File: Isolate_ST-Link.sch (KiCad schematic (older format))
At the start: 54 parts, among them J1 USB_OTG, J2 CONN_01X06, J3 CONN_01X04, J4 CONN_01X02, J5 CONN_01X02, Q1 BSS138, U1 MAU10x, U2 ADuM4160, U3 APE8865NR-33-HF-3

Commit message: 10pin版つくった
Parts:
- removed J2: CONN_01X06, Connector_JST:JST_EH_S06B-EH_1x06_P2.50mm_Horizontal, symbol Isolate_ST-Link-rescue:CONN_01X06
- added J2: Conn_02x05_Odd_Even, Connector_PinHeader_1.27mm:PinHeader_2x05_P1.27mm_Vertical_SMD, symbol Connector_Generic:Conn_02x05_Odd_Even
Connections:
- wire segments 165 -> 177
- no-connect marks 1 -> 3
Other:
- moved on the sheet: R28
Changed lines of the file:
@@
 	1    0    0    -1
-$EndComp
-$Comp
-L Isolate_ST-Link-rescue:CONN_01X06 J2
-U 1 1 5948A2BD
-P 9500 2950
-F 0 "J2" H 9500 3300 50  0000 C CNN
-F 1 "CONN_01X06" V 9600 2950 50  0000 C CNN
-F 2 "Connector_JST:JST_EH_S06B-EH_1x06_P2.50mm_Horizontal" H 9500 2950 50  0001 C CNN
-F 3 "" H 9500 2950 50  0001 C CNN
-	1    9500 2950
-	1    0    0    1
 $EndComp
 Text GLabel 8000 2700 0    60   Input ~ 0
@@
 Text GLabel 8000 2900 0    60   Input ~ 0
 T_JTMS
-$Comp
-L power1:GND #PWR08
-U 1 1 5948BBA0
-P 8800 3250
-F 0 "#PWR08" H 8800 3000 50  0001 C CNN
-F 1 "GND" H 8800 3100 50  0000 C CNN
-F 2 "" H 8800 3250 50  0001 C CNN
-F 3 "" H 8800 3250 50  0001 C CNN
-	1    8800 3250
-	-1   0    0    -1
-$EndComp
-Text GLabel 8000 3100 0    60   Input ~ 0
+Text GLabel 8000 3000 0    60   Input ~ 0
 T_JTCK
 $Comp
@@
 L device:R R28
 U 1 1 59CA9CFA
-P 8550 3100
-F 0 "R28" V 8630 3100 50  0000 C CNN
-F 1 "22" V 8550 3100 50  0000 C CNN
-F 2 "Resistor_SMD:R_0603_1608Metric" V 8480 3100 50  0001 C CNN
-F 3 "" H 8550 3100 50  0001 C CNN
-	1    8550 3100
+P 8550 3000
+F 0 "R28" V 8630 3000 50  0000 C CNN
+F 1 "22" V 8550 3000 50  0000 C CNN
+F 2 "Resistor_SMD:R_0603_1608Metric" V 8480 3000 50  0001 C CNN
+F 3 "" H 8550 3000 50  0001 C CNN
+	1    8550 3000
 	0    -1   1    0
 $EndComp
@@
 Connection ~ 1250 4700
 Wire Wire Line
-	8800 3000 9300 3000
-Wire Wire Line
 	6150 4800 6200 4800
 Wire Wire Line
 	6200 5100 6150 5100
 Wire Wire Line
-	7450 3200 8900 3200
+	7450 3200 9700 3200
 Wire Wire Line
 	8000 2900 8100 2900
@@
 Connection ~ 1600 4050
 Wire Wire Line
-	8700 3100 9000 3100
+	8700 3000 9000 3000
 Wire Wire Line
 	8400 2900 9100 2900
@@
 	8800 2000 9200 2000
 Wire Wire Line
-	8900 2450 8900 3200
-Connection ~ 8900 3200
-Wire Wire Line
-	8400 2700 9300 2700
+	9700 2450 9700 3200
 Wire Wire Line
 	9200 2000 9200 2800
-Connection ~ 9200 2800
 Wire Wire Line
 	9100 2150 9100 2900
-Connection ~ 9100 2900
-Wire Wire Line
-	9000 2300 9000 3100
-Connection ~ 9000 3100
+Wire Wire Line
+	9000 2300 9000 3000
 Wire Notes Line
 	3800 2400 3800 5050
@@
 Connection ~ 6200 4800
 Wire Wire Line
-	8000 3100 8400 3100
-Wire Wire Line
-	8900 2450 8800 2450
+	8000 3000 8400 3000
+Wire Wire Line
+	9700 2450 8800 2450
 Wire Wire Line
 	8500 2450 7700 2450
@@
 	7700 2450 7700 1800
 Wire Wire Line
-	8800 3250 8800 3000
-Wire Wire Line
 	8150 4450 8750 4450
 Wire Wire Line
@@
 	1600 4050 1650 4050
 Wire Wire Line
-	8900 3200 9300 3200
-Wire Wire Line
-	9200 2800 9300 2800
-Wire Wire Line
-	9100 2900 9300 2900
-Wire Wire Line
-	9000 3100 9300 3100
-Wire Wire Line
 	9000 3700 9000 4350
 Wire Wire Line
@@
 Wire Wire Line
 	6200 4800 6200 5100
+$Comp
+L Connector_Generic:Conn_02x05_Odd_Even J2
+U 1 1 5C6B4233
+P 10100 3400
+F 0 "J2" H 10150 3817 50  0000 C CNN
+F 1 "Conn_02x05_Odd_Even" H 10150 3726 50  0000 C CNN
+F 2 "Connector_PinHeader_1.27mm:PinHeader_2x05_P1.27mm_Vertical_SMD" H 10100 3400 50  0001 C CNN
+F 3 "~" H 10100 3400 50  0001 C CNN
+	1    10100 3400
+	1    0    0    -1
+$EndComp
+$Comp
+L power1:GND #PWR0101
+U 1 1 5C6B457F
+P 9800 3650
+F 0 "#PWR0101" H 9800 3400 50  0001 C CNN
+F 1 "GND" H 9800 3500 50  0000 C CNN
+F 2 "" H 9800 3650 50  0001 C CNN
+F 3 "" H 9800 3650 50  0001 C CNN
+	1    9800 3650
+	-1   0    0    -1
+$EndComp
+NoConn ~ 9900 3500
+Wire Wire Line
+	9900 3600 9800 3600
+Wire Wire Line
+	9800 3600 9800 3650
+Wire Wire Line
+	9900 3400 9800 3400
+Wire Wire Line
+	9800 3400 9800 3600
+Connection ~ 9800 3600
+Wire Wire Line
+	9900 3300 9800 3300
+Wire Wire Line
+	9800 3300 9800 3400
+Connection ~ 9800 3400
+Wire Wire Line
+	9200 2000 10900 2000
+Wire Wire Line
+	10900 2000 10900 3600
+Wire Wire Line
+	10900 3600 10400 3600
+Connection ~ 9200 2000
+Wire Wire Line
+	9100 2150 10800 2150
+Wire Wire Line
+	10800 2150 10800 3200
+Wire Wire Line
+	10800 3200 10400 3200
+Connection ~ 9100 2150
+Wire Wire Line
+	9000 2300 10700 2300
+Wire Wire Line
+	10700 2300 10700 3300
+Wire Wire Line
+	10700 3300 10400 3300
+Connection ~ 9000 2300
+Wire Wire Line
+	10600 2700 10600 3400
+Wire Wire Line
+	10600 3400 10400 3400
+NoConn ~ 10400 3500
+Wire Wire Line
+	9700 3200 9900 3200
+Connection ~ 9700 3200
+Wire Wire Line
+	8400 2700 10600 2700
 $EndSCHEMATC

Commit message: USBをType-Cに
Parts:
- removed J1: USB_OTG, Connector_USB:USB_Micro-B_Molex-105017-0001, symbol Isolate_ST-Link-rescue:USB_OTG
- added J7: USB_C_Receptacle_USB2.0, Connector_USB:USB_C_Receptacle_GCT_USB4085, symbol Connector:USB_C_Receptacle_USB2.0
- added R35: 5.1k, Resistor_SMD:R_0603_1608Metric, symbol device:R
- R1: value 100k -> 5.1k
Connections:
- wire segments 177 -> 200
- no-connect marks 3 -> 5
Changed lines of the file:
@@
 EESchema Schematic File Version 4
 LIBS:Isolate_ST-Link-cache
-EELAYER 26 0
+EELAYER 29 0
 EELAYER END
 $Descr A4 11693 8268
@@
 $EndSheet
 $Comp
-L Isolate_ST-Link-rescue:USB_OTG J1
-U 1 1 5948518F
-P 1250 4250
-F 0 "J1" H 1050 4700 50  0000 L CNN
-F 1 "USB_OTG" H 1050 4600 50  0000 L CNN
-F 2 "Connector_USB:USB_Micro-B_Molex-105017-0001" H 1400 4200 50  0001 C CNN
-F 3 "" H 1400 4200 50  0001 C CNN
-	1    1250 4250
-	1    0    0    -1
-$EndComp
-$Comp
 L device:D_Zener_Small D3
 U 1 1 59485C1F
@@
 	1    0    0    -1
 $EndComp
-$Comp
-L power1:GNDPWR #PWR07
-U 1 1 59488AEA
-P 1250 4850
-F 0 "#PWR07" H 1250 4650 50  0001 C CNN
-F 1 "GNDPWR" H 1250 4720 50  0000 C CNN
-F 2 "" H 1250 4800 50  0001 C CNN
-F 3 "" H 1250 4800 50  0001 C CNN
-	1    1250 4850
-	1    0    0    -1
-$EndComp
 Text GLabel 8000 2700 0    60   Input ~ 0
 T_SWO
@@
 $EndComp
 $Comp
-L device:R R1
-U 1 1 594A71FB
-P 1600 4650
-F 0 "R1" V 1680 4650 50  0000 C CNN
-F 1 "100k" V 1600 4650 50  0000 C CNN
-F 2 "Resistor_SMD:R_0603_1608Metric" V 1530 4650 50  0001 C CNN
-F 3 "" H 1600 4650 50  0001 C CNN
-	1    1600 4650
-	1    0    0    -1
-$EndComp
-$Comp
-L power1:GNDPWR #PWR019
-U 1 1 594A7A10
-P 1600 4850
-F 0 "#PWR019" H 1600 4650 50  0001 C CNN
-F 1 "GNDPWR" H 1600 4720 50  0000 C CNN
-F 2 "" H 1600 4800 50  0001 C CNN
-F 3 "" H 1600 4800 50  0001 C CNN
-	1    1600 4850
-	1    0    0    -1
-$EndComp
-$Comp
 L device:R R3
 U 1 1 594A7FD2
@@
 	9000 4350 9050 4350
 Wire Wire Line
-	1250 4650 1250 4700
-Wire Wire Line
-	1150 4650 1150 4700
-Wire Wire Line
-	1150 4700 1250 4700
-Connection ~ 1250 4700
-Wire Wire Line
 	6150 4800 6200 4800
 Wire Wire Line
@@
 	3350 3150 3350 3200
 Wire Wire Line
-	1550 4450 1600 4450
-Wire Wire Line
-	1600 4450 1600 4500
-Wire Wire Line
-	1600 4850 1600 4800
-Wire Wire Line
-	1800 4350 1550 4350
-Wire Wire Line
-	1800 4250 1550 4250
+	1800 4350 1750 4350
+Wire Wire Line
+	1800 4250 1750 4250
 Wire Wire Line
 	2250 4350 2100 4350
 Wire Wire Line
 	2100 4250 3350 4250
-Wire Wire Line
-	1550 4050 1600 4050
 Wire Wire Line
 	2000 4050 1950 4050
@@
 Wire Wire Line
 	7900 4550 7900 4600
-Wire Wire Line
-	1250 4700 1250 4850
 Wire Wire Line
 	4700 4350 4700 4400
@@
 Wire Wire Line
 	8400 2700 10600 2700
+$Comp
+L Connector:USB_C_Receptacle_USB2.0 J7
+U 1 1 5CC5CAFE
+P 1250 6000
+F 0 "J7" H 1357 6867 50  0000 C CNN
+F 1 "USB_C_Receptacle_USB2.0" H 1357 6776 50  0000 C CNN
+F 2 "Connector_USB:USB_C_Receptacle_GCT_USB4085" H 1400 6000 50  0001 C CNN
+F 3 "https://www.usb.org/sites/default/files/documents/usb_type-c.zip" H 1400 6000 50  0001 C CNN
+	1    1250 6000
+	1    0    0    -1
+$EndComp
+Wire Wire Line
+	1850 5400 2100 5400
+Wire Wire Line
+	2100 5400 2100 4550
+Wire Wire Line
+	2100 4550 1700 4550
+Wire Wire Line
+	1700 4550 1700 4150
+Wire Wire Line
+	1700 4150 1600 4150
+Wire Wire Line
+	1600 4150 1600 4050
+$Comp
+L power:GNDPWR #PWR0102
+U 1 1 5CC728CF
+P 1250 7050
+F 0 "#PWR0102" H 1250 6850 50  0001 C CNN
+F 1 "GNDPWR" H 1254 6896 50  0000 C CNN
+F 2 "" H 1250 7000 50  0001 C CNN
+F 3 "" H 1250 7000 50  0001 C CNN
+	1    1250 7050
+	1    0    0    -1
+$EndComp
+Wire Wire Line
+	1250 7050 1250 6950
+Wire Wire Line
+	950  6900 950  6950
+Wire Wire Line
+	950  6950 1250 6950
+Connection ~ 1250 6950
+Wire Wire Line
+	1250 6950 1250 6900
+Wire Wire Line
+	1850 5900 1950 5900
+Wire Wire Line
+	1950 5900 1950 6000
+Wire Wire Line
+	1950 6000 1850 6000
+Wire Wire Line
+	1850 6100 1950 6100
+Wire Wire Line
+	1950 6100 1950 6200
+Wire Wire Line
+	1950 6200 1850 6200
+Wire Wire Line
+	1950 5900 1950 4500
+Wire Wire Line
+	1950 4500 1750 4500
+Wire Wire Line
+	1750 4500 1750 4350
+Connection ~ 1950 5900
+Wire Wire Line
+	1950 6100 2300 6100
+Wire Wire Line
+	2300 6100 2300 4050
+Wire Wire Line
+	2300 4050 2100 4050
+Wire Wire Line
+	2100 4050 2100 4150
+Wire Wire Line
+	2100 4150 1750 4150
+Wire Wire Line
+	1750 4150 1750 4250
+Connection ~ 1950 6100
+NoConn ~ 1850 6500
+NoConn ~ 1850 6600
+$Comp
+L device:R R35
+U 1 1 5CC654E2
+P 2900 5600
+F 0 "R35" V 2693 5600 50  0000 C CNN
+F 1 "5.1k" V 2784 5600 50  0000 C CNN
+F 2 "Resistor_SMD:R_0603_1608Metric" V 2830 5600 50  0001 C CNN
+F 3 "" H 2900 5600 50  0001 C CNN
+	1    2900 5600
+	0    1    1    0
+$EndComp
+Wire Wire Line
+	2750 5600 1850 5600
+Wire Wire Line
+	1850 5700 2450 5700
+$Comp
+L power:GND #PWR0103
+U 1 1 5CC9433B
+P 3100 5900
+F 0 "#PWR0103" H 3100 5650 50  0001 C CNN
+F 1 "GND" H 3105 5727 50  0000 C CNN
+F 2 "" H 3100 5900 50  0001 C CNN
+F 3 "" H 3100 5900 50  0001 C CNN
+	1    3100 5900
+	1    0    0    -1
+$EndComp
+Wire Wire Line
+	3100 5600 3050 5600
+Wire Wire Line
+	3100 5600 3100 5700
+Wire Wire Line
+	2750 5700 3100 5700
+Connection ~ 3100 5700
+Wire Wire Line
+	3100 5700 3100 5900
+$Comp
+L device:R R1
+U 1 1 5CCB9E94
+P 2600 5700
+F 0 "R1" V 2393 5700 50  0000 C CNN
+F 1 "5.1k" V 2484 5700 50  0000 C CNN
+F 2 "Resistor_SMD:R_0603_1608Metric" V 2530 5700 50  0001 C CNN
+F 3 "" H 2600 5700 50  0001 C CNN
+	1    2600 5700
+	0    1    1    0
+$EndComp
 $EndSCHEMATC

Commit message: 最低限の配線はできたんじゃね
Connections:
- net labels added: DIN_+, DIN_-, UD+, UD-
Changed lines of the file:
@@
 Wire Wire Line
 	1850 5700 2450 5700
-$Comp
-L power:GND #PWR0103
-U 1 1 5CC9433B
-P 3100 5900
-F 0 "#PWR0103" H 3100 5650 50  0001 C CNN
-F 1 "GND" H 3105 5727 50  0000 C CNN
-F 2 "" H 3100 5900 50  0001 C CNN
-F 3 "" H 3100 5900 50  0001 C CNN
-	1    3100 5900
-	1    0    0    -1
-$EndComp
 Wire Wire Line
 	3100 5600 3050 5600
@@
 	0    1    1    0
 $EndComp
+Text Label 1950 4800 0    50   ~ 0
+DIN_-
+Text Label 2300 4800 0    50   ~ 0
+DIN_+
+Text Label 2550 4150 0    50   ~ 0
+UD-
+Text Label 2550 4250 0    50   ~ 0
+UD+
+$Comp
+L power:GNDPWR #PWR?
+U 1 1 5CD2DF7B
+P 3100 5900
+F 0 "#PWR?" H 3100 5700 50  0001 C CNN
+F 1 "GNDPWR" H 3104 5746 50  0000 C CNN
+F 2 "" H 3100 5850 50  0001 C CNN
+F 3 "" H 3100 5850 50  0001 C CNN
+	1    3100 5900
+	1    0    0    -1
+$EndComp
 $EndSCHEMATC

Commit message: DCDCをRECOMのものに変更
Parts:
- removed U1: MAU10x, Converter_DCDC(my):DCDC-Conv_Minimax_MAU10x, symbol mylib:MAU10x
- added U1: RFM-0505S, Converter_DCDC_my:Converter_DCDC_RECOM_RFM-0505S-0.2_THT, symbol mylib:RFM-0505S
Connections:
- net +5V: now also U1.4 (+Vout)
- net +5VP: now also U1.2 (+Vin)
- net GND: now also U1.3 (-Vout)
- net GNDPWR: now also U1.1 (-Vin)
- no-connect marks 5 -> 4
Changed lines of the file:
@@
-$EndComp
-$Comp
-L mylib:MAU10x U1
-U 1 1 5949C30A
-P 3800 3050
-F 0 "U1" H 4050 3300 60  0000 C CNN
-F 1 "MAU10x" H 3650 3300 60  0000 C CNN
-F 2 "Converter_DCDC(my):DCDC-Conv_Minimax_MAU10x" H 3500 3250 60  0001 C CNN
-F 3 "" H 3500 3250 60  0001 C CNN
-	1    3800 3050
-	1    0    0    -1
 $EndComp
 $Comp
@@
 	1    0    0    -1
 $EndComp
-NoConn ~ 4200 3050
 $Comp
 L power1:GNDPWR #PWR014
@@
 UD+
 $Comp
-L power:GNDPWR #PWR?
+L power:GNDPWR #PWR0103
 U 1 1 5CD2DF7B
 P 3100 5900
-F 0 "#PWR?" H 3100 5700 50  0001 C CNN
+F 0 "#PWR0103" H 3100 5700 50  0001 C CNN
 F 1 "GNDPWR" H 3104 5746 50  0000 C CNN
 F 2 "" H 3100 5850 50  0001 C CNN
@@
 	1    0    0    -1
 $EndComp
+$Comp
+L mylib:RFM-0505S U1
+U 1 1 5CD8A452
+P 3800 3050
+F 0 "U1" H 3800 3437 60  0000 C CNN
+F 1 "RFM-0505S" H 3800 3331 60  0000 C CNN
+F 2 "Converter_DCDC_my:Converter_DCDC_RECOM_RFM-0505S-0.2_THT" H 3500 3250 60  0001 C CNN
+F 3 "http://www.op316.com/tubes/datalib/image/mau100.pdf" H 3500 3250 60  0001 C CNN
+	1    3800 3050
+	1    0    0    -1
+$EndComp

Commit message: 整理
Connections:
- net GNDPWR: now also R1.2, R35.2; no longer R1.1, R35.1
- net at J7.A5 (CC1): now also R35.1; no longer R35.2
- net at J7.B5 (CC2): now also R1.1; no longer R1.2
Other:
- moved on the sheet: C1, C2, C3, C4, C5, C6, C7, D1, D10, D2, D3, D4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

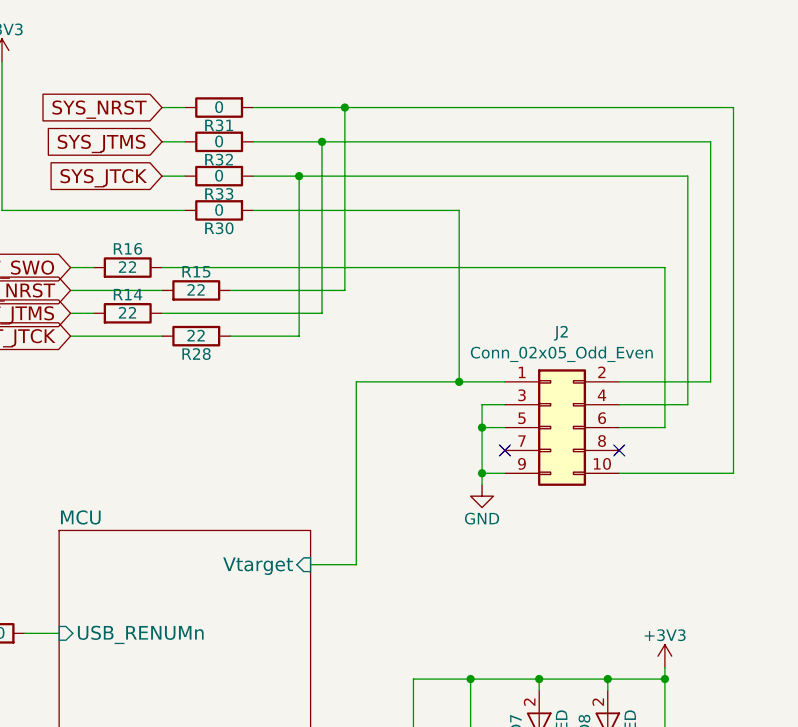
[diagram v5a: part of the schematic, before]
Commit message: EHコネクタ版
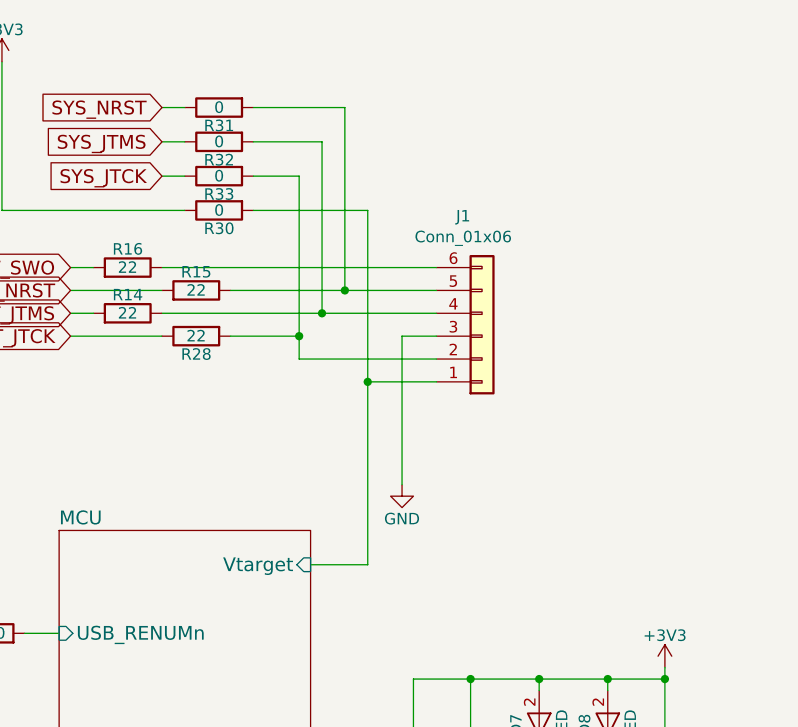
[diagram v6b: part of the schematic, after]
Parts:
- removed J2: Conn_02x05_Odd_Even, Connector_PinHeader_1.27mm:PinHeader_2x05_P1.27mm_Vertical_SMD, symbol Connector_Generic:Conn_02x05_Odd_Even
- added J1: Conn_01x06, Connector_JST:JST_EH_S6B-EH_1x06_P2.50mm_Horizontal, symbol Connector_Generic:Conn_01x06
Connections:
- net GND: now also J1.3 (Pin_3)
- net MCU/Vtarget: now also J1.1 (Pin_1)
- net at R14.1, R32.2: now also J1.4 (Pin_4)
- net at R15.1, R31.2: now also J1.5 (Pin_5)
- net at R16.1: now also J1.6 (Pin_6)
- net at R28.2, R33.2: now also J1.2 (Pin_2)
- no-connect marks 4 -> 2
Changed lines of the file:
@@
 	8400 1000 8800 1000
 Wire Wire Line
-	9300 1450 9300 2200
+	8900 1450 8900 2200
 Wire Wire Line
 	8800 1000 8800 1800
@@
 	7600 2000 8000 2000
 Wire Wire Line
-	9300 1450 8400 1450
+	8900 1450 8400 1450
 Wire Wire Line
 	8100 1450 7300 1450
@@
 Wire Wire Line
 	7400 4600 7400 4900
-$Comp
-L Connector_Generic:Conn_02x05_Odd_Even J2
-U 1 1 5C6B4233
-P 9700 2400
-F 0 "J2" H 9750 2817 50  0000 C CNN
-F 1 "Conn_02x05_Odd_Even" H 9750 2726 50  0000 C CNN
-F 2 "Connector_PinHeader_1.27mm:PinHeader_2x05_P1.27mm_Vertical_SMD" H 9700 2400 50  0001 C CNN
-F 3 "~" H 9700 2400 50  0001 C CNN
-	1    9700 2400
-	1    0    0    -1
-$EndComp
 $Comp
 L power1:GND #PWR0101
 U 1 1 5C6B457F
-P 9400 2650
-F 0 "#PWR0101" H 9400 2400 50  0001 C CNN
-F 1 "GND" H 9400 2500 50  0000 C CNN
-F 2 "" H 9400 2650 50  0001 C CNN
-F 3 "" H 9400 2650 50  0001 C CNN
-	1    9400 2650
+P 9050 2650
+F 0 "#PWR0101" H 9050 2400 50  0001 C CNN
+F 1 "GND" H 9050 2500 50  0000 C CNN
+F 2 "" H 9050 2650 50  0001 C CNN
+F 3 "" H 9050 2650 50  0001 C CNN
+	1    9050 2650
 	-1   0    0    -1
 $EndComp
-NoConn ~ 9500 2500
-Wire Wire Line
-	9500 2600 9400 2600
-Wire Wire Line
-	9400 2600 9400 2650
-Wire Wire Line
-	9500 2400 9400 2400
-Wire Wire Line
-	9400 2400 9400 2600
-Connection ~ 9400 2600
-Wire Wire Line
-	9500 2300 9400 2300
-Wire Wire Line
-	9400 2300 9400 2400
-Connection ~ 9400 2400
-Wire Wire Line
-	8800 1000 10500 1000
-Wire Wire Line
-	10500 1000 10500 2600
-Wire Wire Line
-	10500 2600 10000 2600
-Connection ~ 8800 1000
-Wire Wire Line
-	8700 1150 10400 1150
-Wire Wire Line
-	10400 1150 10400 2200
-Wire Wire Line
-	10400 2200 10000 2200
-Connection ~ 8700 1150
-Wire Wire Line
-	8600 1300 10300 1300
-Wire Wire Line
-	10300 1300 10300 2300
-Wire Wire Line
-	10300 2300 10000 2300
-Connection ~ 8600 1300
-Wire Wire Line
-	10200 1700 10200 2400
-Wire Wire Line
-	10200 2400 10000 2400
-NoConn ~ 10000 2500
-Wire Wire Line
-	9300 2200 9500 2200
-Connection ~ 9300 2200
-Wire Wire Line
-	8000 1700 10200 1700
+Connection ~ 8900 2200
 $Comp
 L Connector:USB_C_Receptacle_USB2.0 J7
@@
 	2450 4900 2650 4900
 Wire Wire Line
-	8650 3000 8850 3000
-Wire Wire Line
-	8850 3000 8850 2200
-Wire Wire Line
-	8850 2200 9300 2200
+	8650 3000 8900 3000
+Wire Wire Line
+	8900 3000 8900 2200
+$Comp
+L Connector_Generic:Conn_01x06 J1
+U 1 1 5D0275EA
+P 9400 2000
+F 0 "J1" H 9318 1475 50  0000 C CNN
+F 1 "Conn_01x06" H 9318 1566 50  0000 C CNN
+F 2 "Connector_JST:JST_EH_S6B-EH_1x06_P2.50mm_Horizontal" H 9400 2000 50  0001 C CNN
+F 3 "~" H 9400 2000 50  0001 C CNN
+	1    9400 2000
+	1    0    0    1
+$EndComp
+Connection ~ 8600 2000
+Connection ~ 8800 1800
+Connection ~ 8700 1900
+Wire Wire Line
+	9200 2000 9050 2000
+Wire Wire Line
+	9050 2000 9050 2650
+Wire Wire Line
+	8900 2200 9200 2200
+Wire Wire Line
+	8700 1900 9200 1900
+Wire Wire Line
+	8800 1800 9200 1800
+Wire Wire Line
+	9200 2100 8600 2100
+Wire Wire Line
+	8600 2100 8600 2000
+Wire Wire Line
+	8000 1700 9200 1700
 $EndSCHEMATC

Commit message: viaうち職人
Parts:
- R1, R35: footprint Resistor_SMD:R_0603_1608Metric -> Resistor_SMD:R_0402_1005Metric
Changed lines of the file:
@@
 F 0 "R1" V 2093 4700 50  0000 C CNN
 F 1 "5.1k" V 2184 4700 50  0000 C CNN
-F 2 "Resistor_SMD:R_0603_1608Metric" V 2230 4700 50  0001 C CNN
+F 2 "Resistor_SMD:R_0402_1005Metric" V 2230 4700 50  0001 C CNN
 F 3 "" H 2300 4700 50  0001 C CNN
 	1    2300 4700
@@
 F 0 "R35" V 2443 4700 50  0000 C CNN
 F 1 "5.1k" V 2534 4700 50  0000 C CNN
-F 2 "Resistor_SMD:R_0603_1608Metric" V 2580 4700 50  0001 C CNN
+F 2 "Resistor_SMD:R_0402_1005Metric" V 2580 4700 50  0001 C CNN
 F 3 "" H 2650 4700 50  0001 C CNN
 	1    2650 4700
